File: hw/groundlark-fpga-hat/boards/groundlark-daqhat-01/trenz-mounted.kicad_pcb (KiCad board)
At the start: 6 copper layers, 85 x 56 mm, 130 parts, among them J1 Raspberry Pi 40-pin, J4 FPGA test UART/reset, J80 LSHM-150-04.0-L-DV-A-S-K-TR, J81 LSHM-150-04.0-L-DV-A-S-K-TR, J82 LSHM-130-04.0-L-DV-A-S-K-TR, J83 1715721, J90 GEO + / - / SHIELD, Q1 2N7002, U1 24LC32A, U100 TMUX1574PWR, U101 TMUX1574PWR, U102 TCA9534PWR, U103 SN74LVC1G10DCKR, U104 TLV809EA30DBZR, U105 TLV809EA30DBZR, U106 SN74LVC1G08DCKR, U11 LSM6DSOTR, U12 LSM6DSOTR, U13 LSM6DSOTR, U22 ADS122C04, U40 TLV1117LV33DCYR, U41 SN74LVC8T245PWR, U42 SN74LVC8T245PWR, U43 ISO1640BDR, U51 TXU0202DCUR, U52 TLV803EA30DBZR

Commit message: Harden Groundlark and Skylark acquisition, power checks and assembly
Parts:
- moved C43 5.50 mm to (129.2, 88.7)
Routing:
- net GND: track 654.3 -> 657.8 mm, vias 67 -> 76
- net SENS_3V3: track 235.7 -> 237.9 mm

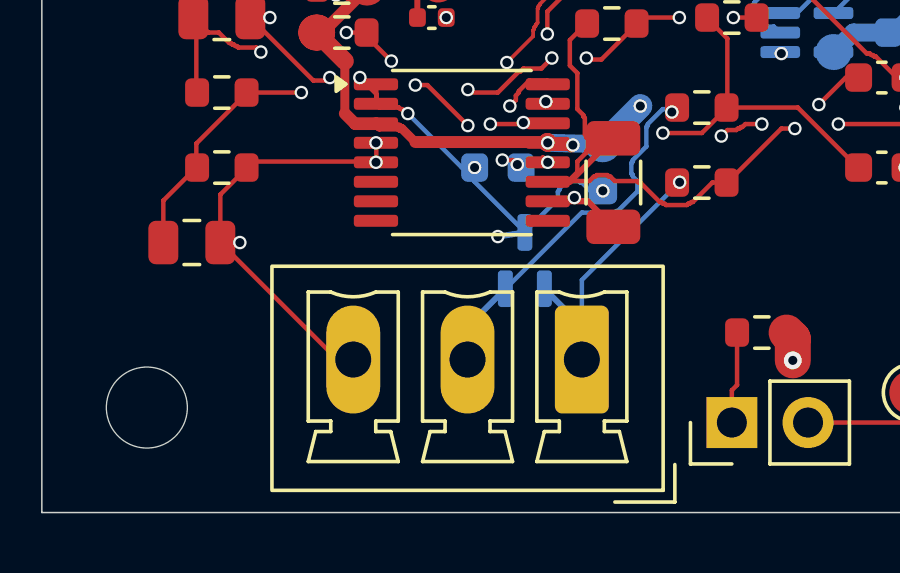
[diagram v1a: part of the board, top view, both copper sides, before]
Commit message: Use horizontal geophone connector and publish detailed enclosure render
Synchronize J90 routing, native SES, assembly mapping, enclosure fit, models and validation. Add a 4K clear-PETG README render and derive assembly PDF part identities from package procurement. Preserve Git-normalized source bindings and original validation/render input hashes. Generated JLCPCB packages remain local.
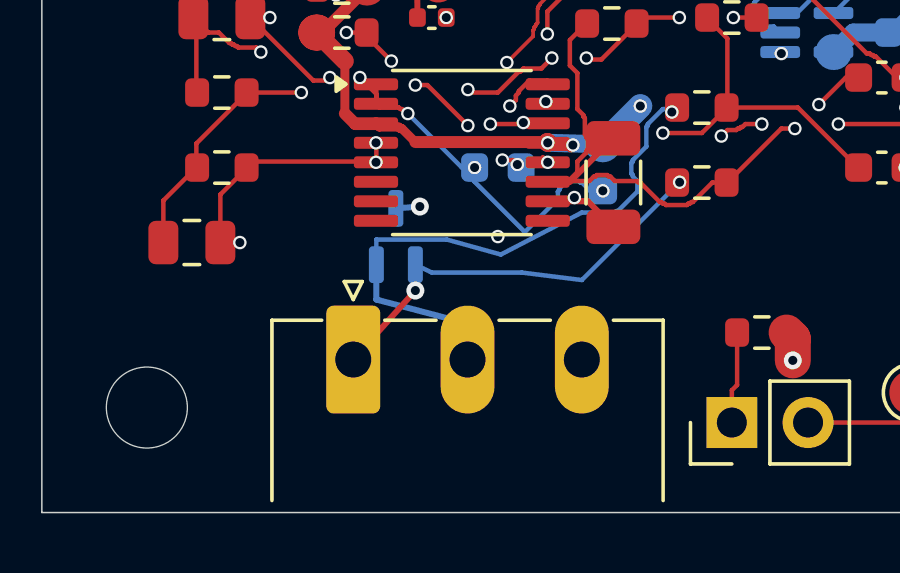
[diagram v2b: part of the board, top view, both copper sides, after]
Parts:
- J90: footprint Groundlark:Connector_Phoenix_MC__PhoenixContact_MCV_1,5_3-G-3.81_1x03_P3.81mm_Vertical -> Groundlark:Connector_Phoenix_MC__PhoenixContact_MC_1,5_3-G-3.81_1x03_P3.81mm_Horizontal
- moved J90 7.62 mm to (60.4, 100.9), turned to 0 degrees
- moved D90 4.37 mm to (61.8, 96.8)
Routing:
- net GND: track 657.8 -> 651.6 mm, vias 76 -> 77
- net GEO_N: track 14.3 -> 19.6 mm
- net GEO_P: track 9.19 -> 14.3 mm, vias 1 -> 2

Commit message: Add TI Pi power supervision and expand DAQHAT enclosure
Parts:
- added C110: 22u, Groundlark:PWR_C_1210_3225Metric, F.Cu at (141.0, 88.0)
- added C111: 22u, Groundlark:PWR_C_1210_3225Metric, F.Cu at (146.0, 88.0)
- added C112: 22u, Groundlark:PWR_C_1210_3225Metric, F.Cu at (151.0, 89.0)
- added C130: 4.7u, Groundlark:SUP_C_0805_2012Metric, F.Cu at (162.0, 86.0)
- added C131: 10u, Groundlark:PWR_C_1206_3216Metric, F.Cu at (161.0, 77.0)
- added C132: 10u, Groundlark:PWR_C_1206_3216Metric, F.Cu at (170.0, 73.0)
- added C133: 10u, Groundlark:PWR_C_1206_3216Metric, F.Cu at (178.0, 73.0)
- added C134: 100n, Groundlark:PWR_C_0603_1608Metric, F.Cu at (174.0, 74.0)
- added C135: 47u, Groundlark:PWR_CP_Elec_6.3x7.7, F.Cu at (185.0, 77.0)
- added C136: 22u, Groundlark:PWR_C_1210_3225Metric, F.Cu at (169.0, 84.0)
- added C137: 22u, Groundlark:PWR_C_1210_3225Metric, F.Cu at (174.0, 84.0)
- added C138: 22u, Groundlark:PWR_C_1210_3225Metric, F.Cu at (179.0, 85.0)
- added C139: 10n, Groundlark:SUP_C_0603_1608Metric, F.Cu at (185.0, 90.0)
- added C140: 10u, Groundlark:SUP_C_0805_2012Metric, F.Cu at (188.0, 84.0)
- added C141: 100n, Groundlark:PWR_C_0603_1608Metric, F.Cu at (167.5, 93.5)
- added C142: 10u, Groundlark:SUP_C_0805_2012Metric, F.Cu at (164.5, 93.0)
- added C143: 470n, Groundlark:SUP_C_0603_1608Metric, F.Cu at (170.0, 89.5)
- added C144: 10n, Groundlark:SUP_C_0603_1608Metric, F.Cu at (164.0, 89.0)
- added C145: 10n, Groundlark:SUP_C_0603_1608Metric, F.Cu at (173.5, 88.0)
- added C24: 100n, Groundlark:Capacitor_SMD__C_0603_1608Metric, B.Cu at (54.5, 78.5)
- added C86: 10u, Groundlark:PWR_C_1206_3216Metric, F.Cu at (141.0, 77.0)
- added C87: 10u, Groundlark:PWR_C_1206_3216Metric, F.Cu at (149.0, 77.0)
- added C88: 100n, Groundlark:PWR_C_0603_1608Metric, F.Cu at (145.0, 78.0)
- added C89: 47u, Groundlark:PWR_CP_Elec_6.3x7.7, F.Cu at (155.0, 95.0)
- added D130: B340A, Groundlark:PWR_D_SMA, F.Cu at (170.0, 69.0)
- added D131: SMAJ18A, Groundlark:SUP_D_SMA, F.Cu at (185.0, 68.0)
- added D80: B340A, Groundlark:PWR_D_SMA, F.Cu at (145.0, 71.0)
- added D81: SMAJ15A, Groundlark:PWR_D_SMA, F.Cu at (154.0, 73.0)
- added F130: 4A fast, Groundlark:SUP_Fuse_1206_3216Metric, F.Cu at (163.0, 66.0)
- added J130: PI BATTERY 8-18V, Groundlark:SUP_PhoenixContact_MC_1,5_2-G-3.81_1x02_P3.81mm_Horizontal, F.Cu at (170.0, 60.0)
- added J131: SWD / 3V3 REF, Groundlark:SUP_PinHeader_1x05_P1.27mm_Vertical, F.Cu at (184.0, 95.0)
- added JP130: BENCH RUN, Groundlark:SUP_PinHeader_1x02_P2.54mm_Vertical, F.Cu at (167.0, 102.0)
- added Q130: 2N7002, Groundlark:SUP_SOT-23, F.Cu at (162.0, 98.0)
- added Q131: 2N7002, Groundlark:SUP_SOT-23, F.Cu at (178.0, 96.0)
- added R120: 10k, Groundlark:PWR_R_0603_1608Metric, F.Cu at (150.0, 84.0)
- added R121: 4.30k, Groundlark:PWR_R_0603_1608Metric, F.Cu at (150.0, 81.0)
- added R122: 100k, Groundlark:PWR_R_0603_1608Metric, F.Cu at (137.0, 77.0)
- added R123: 15k, Groundlark:PWR_R_0603_1608Metric, F.Cu at (137.0, 80.0)
- added R124: 10k, Groundlark:PWR_R_0603_1608Metric, F.Cu at (139.5, 84.0)
- added R130: 10k, Groundlark:PWR_R_0603_1608Metric, F.Cu at (179.0, 80.0)
- added R131: 2.41k, Groundlark:SUP_R_0603_1608Metric, F.Cu at (179.0, 77.0)
- added R132: 100k, Groundlark:PWR_R_0603_1608Metric, F.Cu at (166.0, 77.0)
- added R133: 2k, Groundlark:SUP_R_0603_1608Metric, F.Cu at (187.0, 92.0)
- added R134: 47k, Groundlark:SUP_R_0603_1608Metric, F.Cu at (166.5, 90.0)
- added R135: 1M, Groundlark:SUP_R_0603_1608Metric, F.Cu at (180.0, 90.0)
- added R136: 150k, Groundlark:SUP_R_0603_1608Metric, F.Cu at (177.0, 90.0)
- added R137: 100k, Groundlark:PWR_R_0603_1608Metric, F.Cu at (163.0, 101.0)
- added R138: 10k, Groundlark:PWR_R_0603_1608Metric, F.Cu at (159.0, 101.0)
- added R139: 100k, Groundlark:PWR_R_0603_1608Metric, F.Cu at (178.0, 99.0)
- added R140: 100k, Groundlark:PWR_R_0603_1608Metric, F.Cu at (178.0, 93.0)
- added R141: 10k, Groundlark:PWR_R_0603_1608Metric, F.Cu at (168.0, 98.0)
- added SW80: FPGA OFF / ON, Groundlark:PWR_SW_SPDT_PCM12, F.Cu at (155.0, 60.0)
- added U130: MSPM0L1105, Groundlark:SUP_QFN-32-1EP_5x5mm_P0.5mm_EP3.45x3.45mm, F.Cu at (172.0, 94.0)
- added U131: TPS70933, Groundlark:SUP_SOT-23-5, F.Cu at (163.0, 82.0)
- added U132: TPSM53603, Groundlark:PWR_Texas_B3QFN-14-1EP_5x5.5mm_P0.65mm, F.Cu at (174.0, 78.0)
- added U133: TPS22953, Groundlark:SUP_Texas_WSON10_DQC0010A, F.Cu at (184.0, 86.0)
- added U23: DLVR-F50D, Groundlark:Groundlark__DLVR_E1BS, F.Cu at (51.5, 76.0)
- added U80: TPSM53603, Groundlark:PWR_Texas_B3QFN-14-1EP_5x5.5mm_P0.65mm, F.Cu at (145.0, 82.0)
- F80: value 0467005.NR -> 2A fast; footprint Groundlark:TZ_TZ_FUSE -> Groundlark:PWR_Fuse_1206_3216Metric
- J83: value 1715721 -> 12V DC / CENTER +; footprint Groundlark:TZ_TZ_POWER -> Groundlark:PWR_BarrelJack_CUI_PJ-102AH_Horizontal
- moved J83 90.3 mm to (145.0, 64.1), turned to 180 degrees
- moved F80 72.6 mm to (139.0, 68.0)
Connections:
- net EXT_3V3 renamed EXT_12V
- F80 pad 2: FPGA_VIN -> FUSED_12V
- J1 pad 31: 31 -> PI_SHUTDOWN_N
- J1 pad 33: 33 -> PI_HALTED
- J81 pad 31: j81-31 -> 31
- J81 pad 33: j81-33 -> 33
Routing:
- net PI_5V: track 108.4 -> 490.2 mm, vias 4 -> 12
- net PI_HALTED: track 0.00 -> 110.2 mm, vias 0 -> 4
- net PI_SHUTDOWN_N: track 0.00 -> 89.8 mm, vias 0 -> 6
- net BAT_PROTECTED: track 0.00 -> 64.4 mm, vias 0 -> 2
- net PROTECTED_12V: track 0.00 -> 63.9 mm, vias 0 -> 2
- net SUP_RUN: track 0.00 -> 56.4 mm, vias 0 -> 4
- net BUCK_EN: track 0.00 -> 51.4 mm, vias 0 -> 2
- net SUP_3V3: track 0.00 -> 50.9 mm, vias 0 -> 4
- net PI_3V3: track 237.5 -> 287.2 mm, vias 18 -> 20
- net FPGA_EN1: track 25.0 -> 73.9 mm, vias 1 -> 2
- net BAT_FUSED: track 0.00 -> 36.4 mm, vias 0 -> 2
- net PI_RAW_5V: track 0.00 -> 28.1 mm, vias 0 -> 12
- net SUP_NRST: track 0.00 -> 26.9 mm, vias 0 -> 1
- net FPGA_VIN: track 119.8 -> 95.2 mm, vias 12 -> 17
- net I2C_SDA: track 47.1 -> 68.7 mm, vias 12 -> 14
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- added copper zone on F.Cu, net GND
- added copper zone on B.Cu, net PI_RAW_5V
- added copper zone on F.Cu, net PI_RAW_5V
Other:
- board size 85 x 56 mm -> 140 x 56 mm
- board text added: "+ GND"
- board text added: "12V DC / CENTER +"
- board text added: "FPGA ON/OFF"
- board text added: "FPGA POWER"
- board text added: "PI BAT 8-18V"
- board text removed: "3V3 ONLY"
